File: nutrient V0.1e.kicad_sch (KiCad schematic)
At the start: 84 parts, among them J1 Conn_01x04_Female, J2 Conn_01x04_Female, J3 Conn_01x04_Female, J4 Conn_01x04_Female, J5 Conn_01x04_Female, J6 Conn_01x04_Female, J7 Conn_01x03_Male, J8 Conn_01x03_Male, P1 SolderJumper_2_Open, P2 SolderJumper_2_Bridged, P3 SolderJumper_2_Bridged, Q1 Q_NMOS_DGS, Q10 Q_NMOS_DGS, Q2 Q_NMOS_DGS, Q3 Q_NMOS_DGS, Q4 Q_NMOS_DGS, Q5 Q_NMOS_DGS, Q6 Q_NMOS_DGS, Q7 Q_NMOS_DGS, Q8 2N3904, U1 23LC512, U2 DS1307+, Y1 Crystal_Small

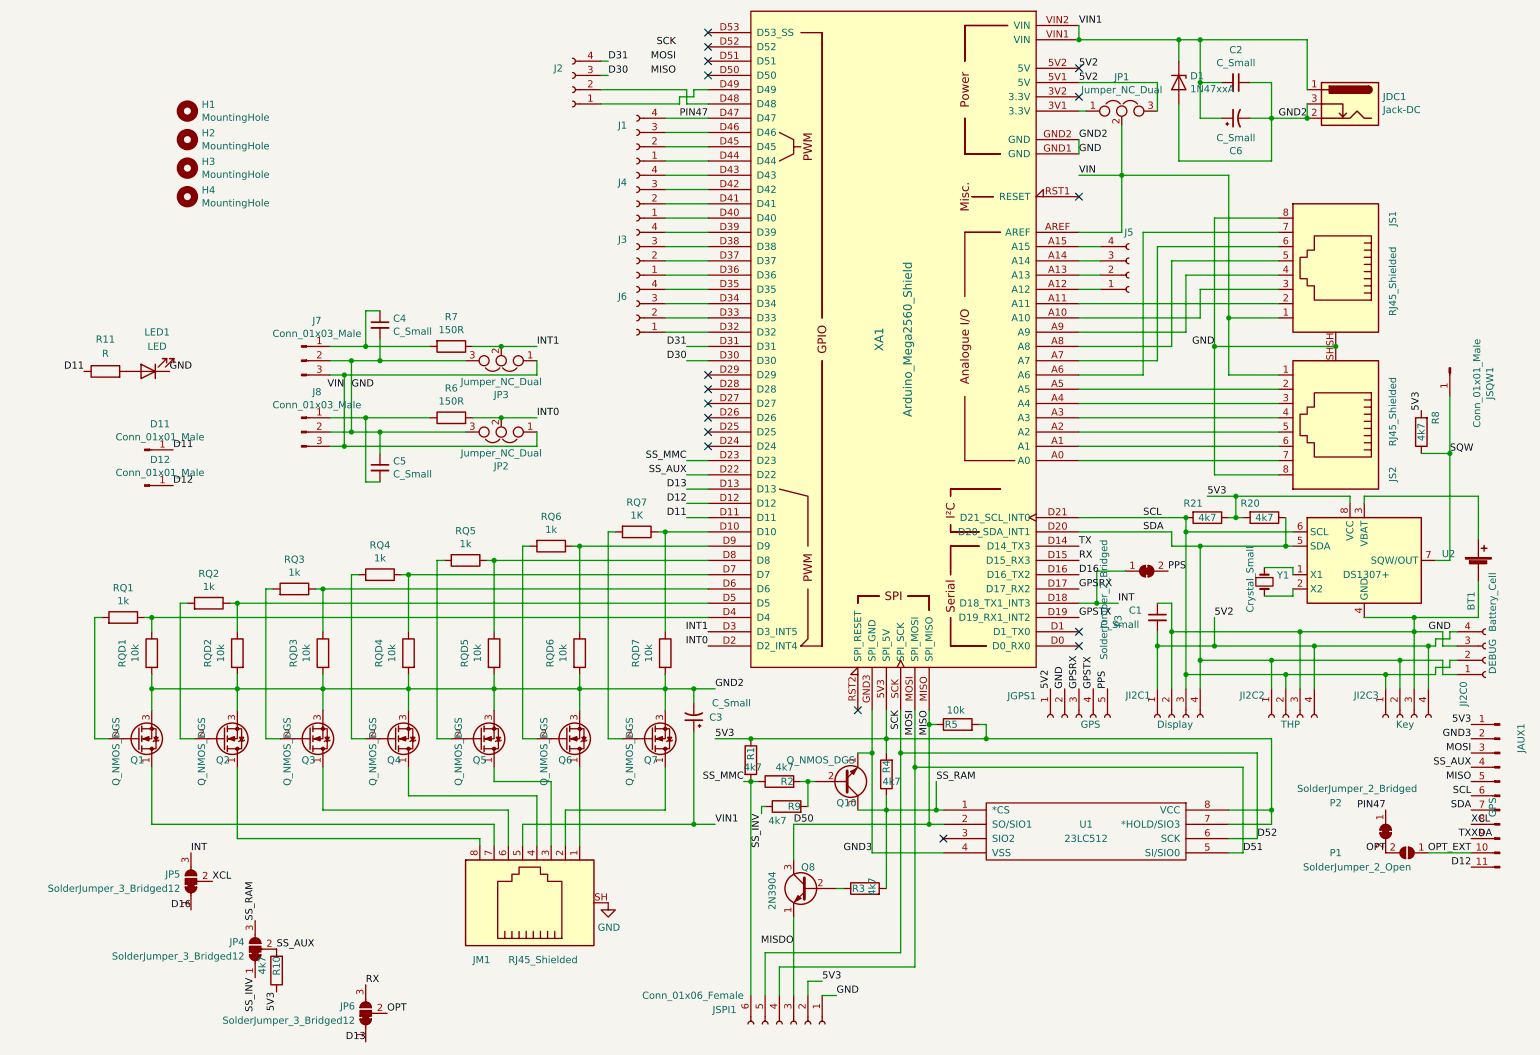
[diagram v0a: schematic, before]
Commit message: Trace changes, GND loop fixes
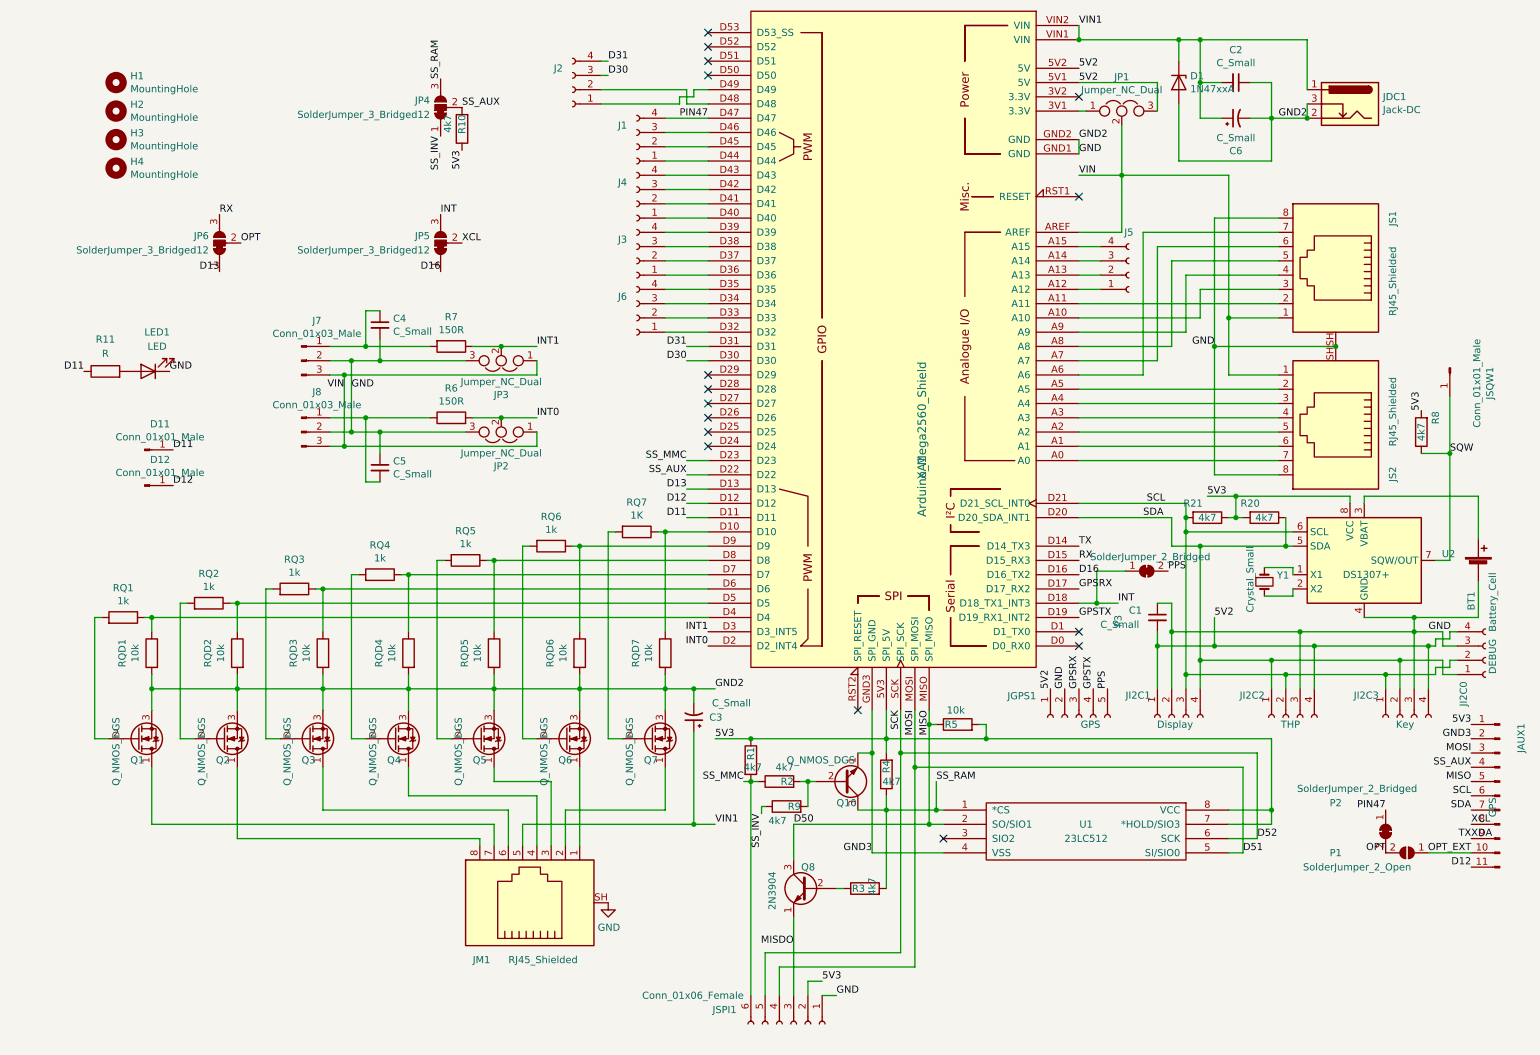
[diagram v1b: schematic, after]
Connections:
- no-connect marks 17 -> 16
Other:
- moved on the sheet: H1, H2, H3, H4, JP4, JP5, JP6, R10
